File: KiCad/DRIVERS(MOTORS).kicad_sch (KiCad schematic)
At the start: 15 parts, among them M1 Motor_DC, M2 Motor_DC, M3 Motor_DC, U7 TB6612FNG, U8 TB6612FNG, U9 TB6612FNG

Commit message: Modificacio Labels
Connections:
- net +12V renamed VBAT
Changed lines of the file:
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@@
 		)
 	)
-	(global_label "+12V"
-		(shape bidirectional)
+	(global_label "VBAT"
+		(shape input)
 		(at 62.23 50.8 180)
 		(fields_autoplaced yes)
@@
 		)
 		(property "Intersheetrefs" "${INTERSHEET_REFS}"
-			(at 53.0535 50.8 0)
+			(at 55.4842 50.8 0)
 			(effects
 				(font
@@
 		)
 	)
-	(global_label "+12V"
-		(shape bidirectional)
+	(global_label "VBAT"
+		(shape input)
 		(at 55.88 60.96 180)
 		(fields_autoplaced yes)
@@
 		)
 		(property "Intersheetrefs" "${INTERSHEET_REFS}"
-			(at 46.7035 60.96 0)
+			(at 49.1342 60.96 0)
 			(effects
 				(font
@@
 		)
 	)
-	(global_label "+12V"
-		(shape bidirectional)
+	(global_label "VBAT"
+		(shape input)
 		(at 54.61 151.13 180)
 		(fields_autoplaced yes)
@@
 		)
 		(property "Intersheetrefs" "${INTERSHEET_REFS}"
-			(at 45.4335 151.13 0)
+			(at 47.8642 151.13 0)
 			(effects
 				(font
@@
 		)
 	)
-	(global_label "+12V"
-		(shape bidirectional)
+	(global_label "VBAT"
+		(shape input)
 		(at 180.34 87.63 180)
 		(fields_autoplaced yes)
@@
 		)
 		(property "Intersheetrefs" "${INTERSHEET_REFS}"
-			(at 171.1635 87.63 0)
-			(effects
-				(font
-					(size 1.27 1.27)
-				)
-				(justify right)
-				(hide yes)
-			)
-		)
-	)
-	(global_label "+12V"
-		(shape bidirectional)
+			(at 173.5942 87.63 0)
+			(effects
+				(font
+					(size 1.27 1.27)
+				)
+				(justify right)
+				(hide yes)
+			)
+		)
+	)
+	(global_label "VBAT"
+		(shape input)
 		(at 242.57 57.15 90)
 		(fields_autoplaced yes)
@@
 		)
 		(property "Intersheetrefs" "${INTERSHEET_REFS}"
-			(at 242.57 47.9735 90)
+			(at 242.57 50.4042 90)
 			(effects
 				(font
@@
 		)
 	)
-	(global_label "+12V"
-		(shape bidirectional)
+	(global_label "VBAT"
+		(shape input)
 		(at 60.96 140.97 180)
 		(fields_autoplaced yes)
@@
 		)
 		(property "Intersheetrefs" "${INTERSHEET_REFS}"
-			(at 51.7835 140.97 0)
-			(effects
-				(font
-					(size 1.27 1.27)
-				)
-				(justify right)
-				(hide yes)
-			)
-		)
-	)
-	(global_label "+12V"
-		(shape bidirectional)
+			(at 54.2142 140.97 0)
+			(effects
+				(font
+					(size 1.27 1.27)
+				)
+				(justify right)
+				(hide yes)
+			)
+		)
+	)
+	(global_label "VBAT"
+		(shape input)
 		(at 186.69 77.47 180)
 		(fields_autoplaced yes)
@@
 		)
 		(property "Intersheetrefs" "${INTERSHEET_REFS}"
-			(at 177.5135 77.47 0)
+			(at 179.9442 77.47 0)
 			(effects
 				(font
@@
 		)
 	)
-	(global_label "+12V"
-		(shape bidirectional)
+	(global_label "VBAT"
+		(shape input)
 		(at 123.19 114.3 90)
 		(fields_autoplaced yes)
@@
 		)
 		(property "Intersheetrefs" "${INTERSHEET_REFS}"
-			(at 123.19 105.1235 90)
-			(effects
-				(font
-					(size 1.27 1.27)
-				)
-				(justify left)
-				(hide yes)
-			)
-		)
-	)
-	(global_label "+12V"
-		(shape bidirectional)
+			(at 123.19 107.5542 90)
+			(effects
+				(font
+					(size 1.27 1.27)
+				)
+				(justify left)
+				(hide yes)
+			)
+		)
+	)
+	(global_label "VBAT"
+		(shape input)
 		(at 120.65 25.4 90)
 		(fields_autoplaced yes)
@@
 		)
 		(property "Intersheetrefs" "${INTERSHEET_REFS}"
-			(at 120.65 16.2235 90)
-			(effects
-				(font
+			(at 120.65 18.6542 90)
+			(effects
+				(font

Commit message: Modificacio
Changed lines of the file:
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@@
 	)
 	(global_label "GND"
-		(shape bidirectional)
+		(shape input)
 		(at 120.65 184.15 270)
 		(fields_autoplaced yes)
@@
 		)
 		(property "Intersheetrefs" "${INTERSHEET_REFS}"
-			(at 120.65 192.117 90)
+			(at 120.65 190.3515 90)
 			(effects
 				(font
@@
 	)
 	(global_label "GND"
-		(shape bidirectional)
+		(shape input)
 		(at 240.03 123.19 270)
 		(fields_autoplaced yes)
@@
 		)
 		(property "Intersheetrefs" "${INTERSHEET_REFS}"
-			(at 240.03 131.157 90)
+			(at 240.03 129.3915 90)
 			(effects
 				(font

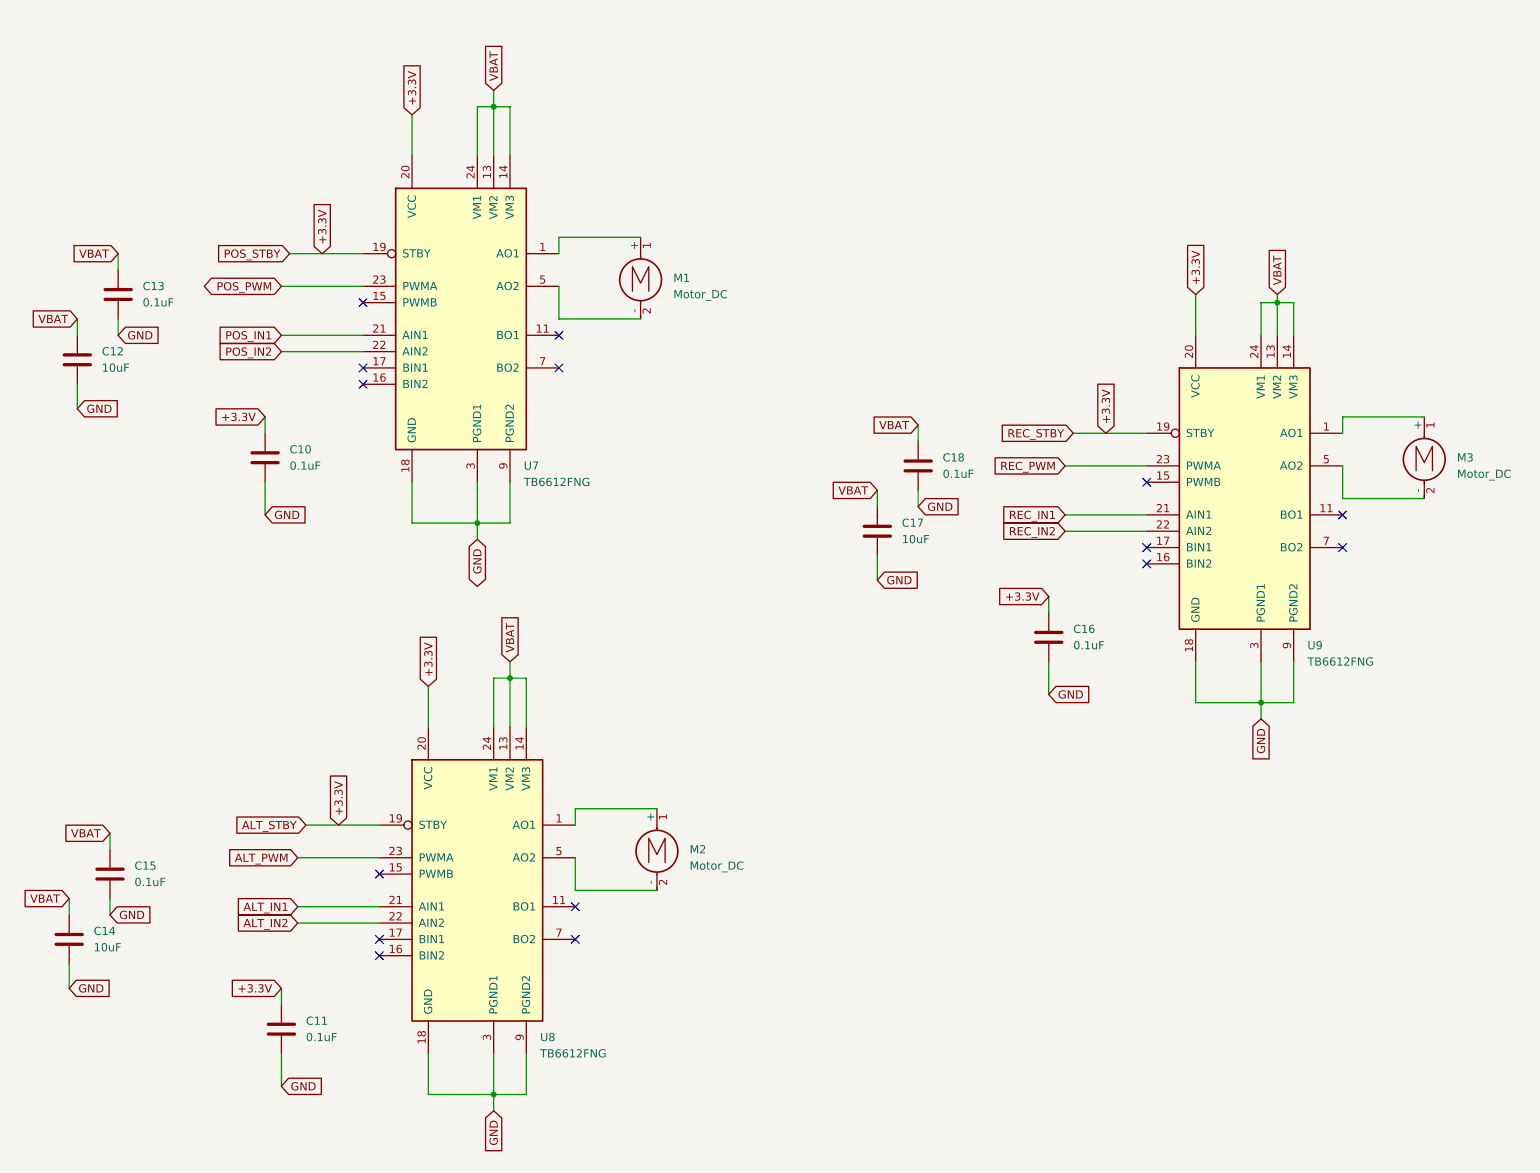
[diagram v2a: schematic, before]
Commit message: cambios mejora ERC
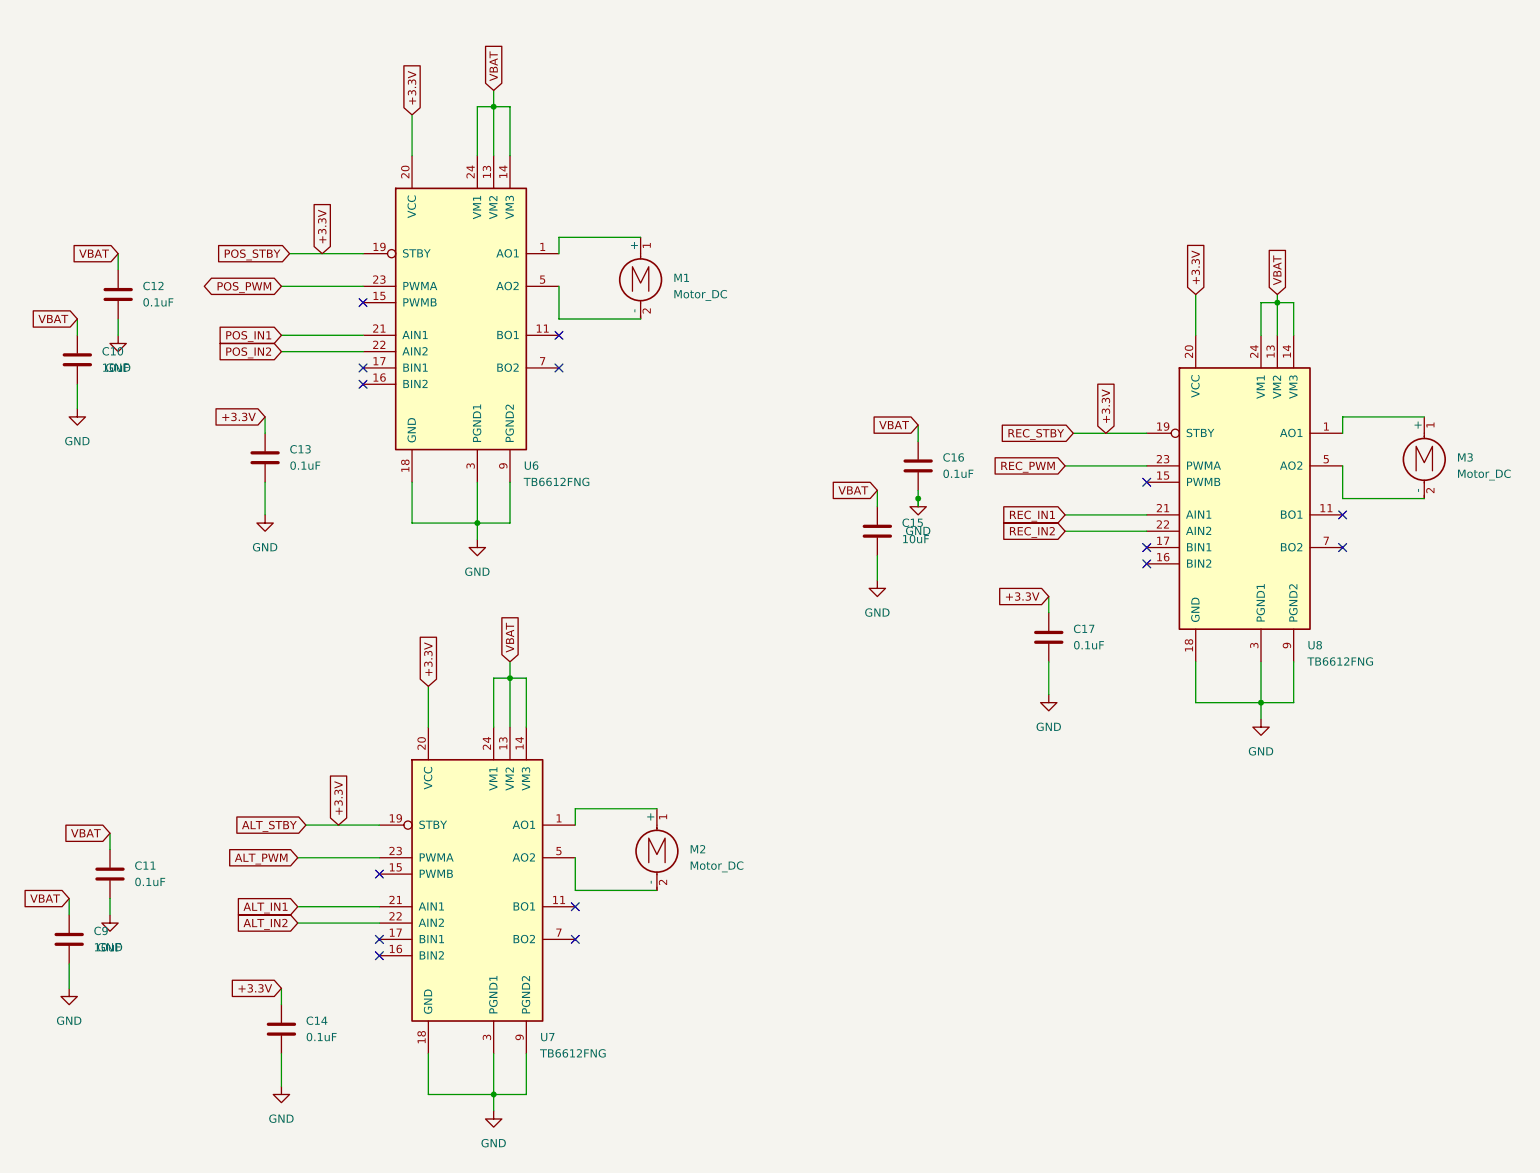
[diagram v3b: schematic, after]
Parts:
- renumbered C12 to C10, C15 to C11, C13 to C12, C10 to C13, C11 to C14, C17 to C15, C18 to C16, C16 to C17, C14 to C9, U7 to U6, U8 to U7, U9 to U8

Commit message: Cambio en la parte de motores y drivers
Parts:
- removed C11, C14, C16, C17: 0.1uF, symbol Device:C
- removed C15, C9: 10uF, symbol Device:C
- removed M3: Motor_DC, symbol Motor:Motor_DC
- removed U7, U8: TB6612FNG, Package_SO:SSOP-24_5.3x8.2mm_P0.65mm, symbol Driver_Motor:TB6612FNG
- added C4: 100nF, symbol Device:C
- added C5: 10uF, symbol Device:C
- added C6: 0.1uF, symbol Device:C
- added M4: Motor_DC, symbol Motor:Motor_DC
- added R1: 10k, symbol Device:R
- added R2, R3: 4.7k, symbol Device:R_US
- added R4, R5: 10k, symbol Device:R_US
- added U2: DRV8871DDA, Package_SO:SSOP-24_5.3x8.2mm_P0.65mm, symbol Driver_Motor:DRV8871DDA
- added U3: ATtiny1616-M, Package_DFN_QFN:VQFN-20-1EP_3x3mm_P0.4mm_EP1.7x1.7mm, symbol MCU_Microchip_ATtiny:ATtiny1616-M
- renumbered C13 to C1, C12 to C2, C10 to C3, U6 to U1
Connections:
- net +3.3V: now also C4.1, R2.1, R3.2, R4.1, R5.1, U3.2 (PA3), U3.4 (VCC)
- net ALT_IN1: now also U2.3 (IN1), U3.12 (PB2)
- net ALT_IN2: now also U2.2 (IN2), U3.11 (PB3)
- net GND: now also C4.2, C5.2, C6.2, R1.2, R4.2, U2.1 (GND), U2.7 (GND), U2.9 (GND), U3.21 (GND), U3.3 (GND)
- net POS_IN1: now also U3.6 (PA5)
- net POS_IN2: now also U3.7 (PA6)
- net POS_PWM: now also U3.5 (PA4)
- net REC_IN1: now also U1.17 (BIN1), U3.14 (PB0)
- net REC_IN2: now also U1.16 (BIN2), U3.13 (PB1)
- net REC_PWM: now also U1.15 (PWMB), U3.8 (PA7)
- net VBAT: now also C5.1, C6.1, U2.5 (VM)
- net at M2.1 (+): now also U1.11 (BO1), U1.12 (BO1)
- net at M2.2 (-): now also U1.7 (BO2), U1.8 (BO2)
- new net: R1.1, U2.4 (ILIM)
- new net: M4.1 (+), U2.6 (OUT1)
- new net: M4.2 (-), U2.8 (OUT2)
- new net MCU_SCL: R3.1, U3.1 (PA2)
- new net MCU_SDA: R2.2, U3.20 (PA1)
- new net UPDI / RESET: R5.2, U3.19 (~{RESET}/PA0)
- no-connect marks 15 -> 6
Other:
- moved on the sheet: C1, C2, C3

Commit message: Modificacions Micro
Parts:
- renumbered C3 to C10, C2 to C12, C1 to C13, C4 to C25, C5 to C26, C6 to C27, M4 to M3, R5 to R16, R3 to R17, R1 to R18, R4 to R19, R2 to R20, U3 to U11, U2 to U12, U1 to U6

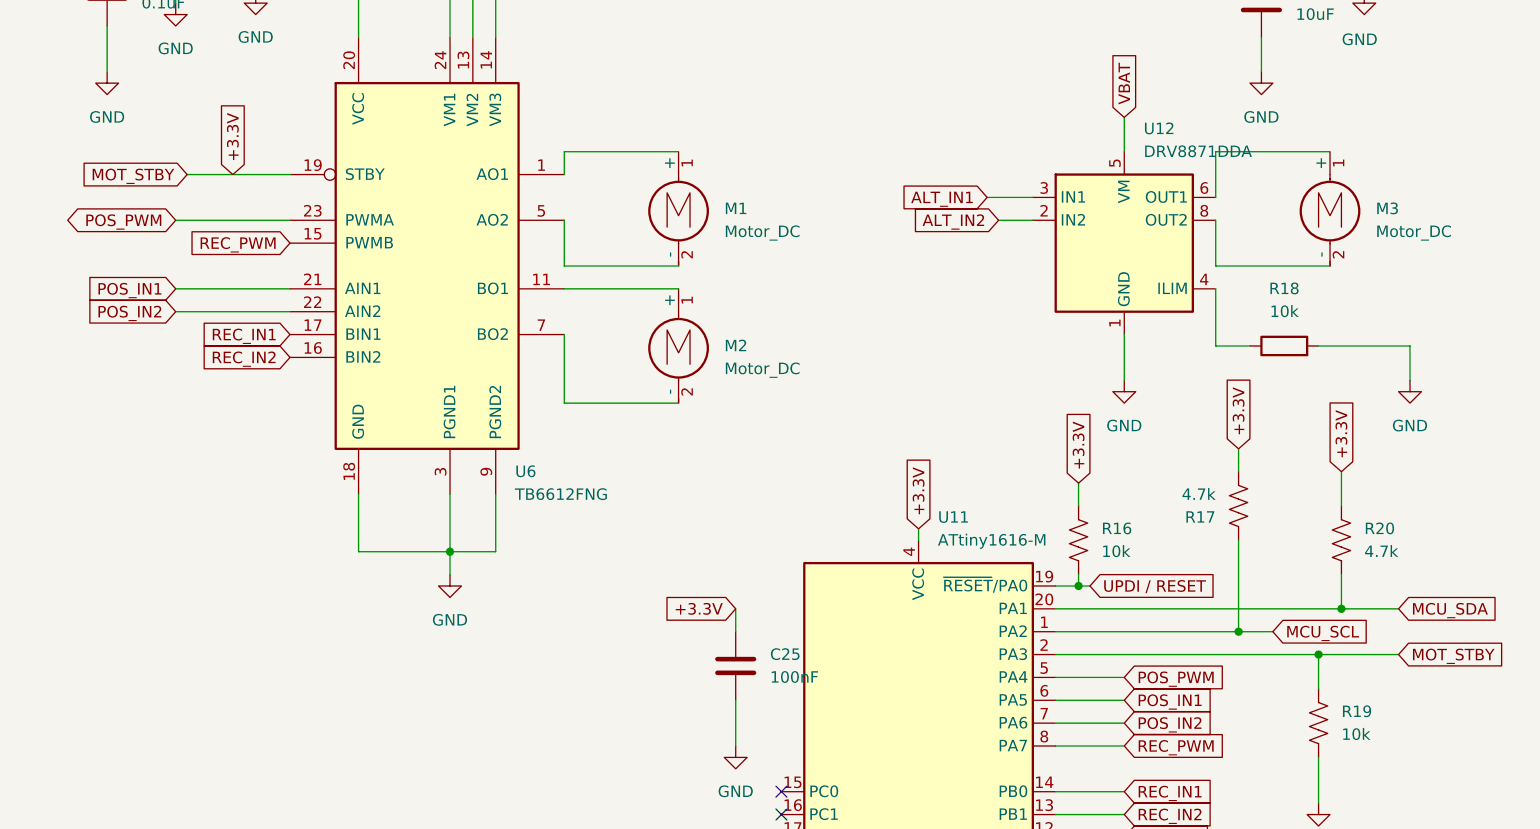
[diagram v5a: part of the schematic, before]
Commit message: Començat el LAYOUT
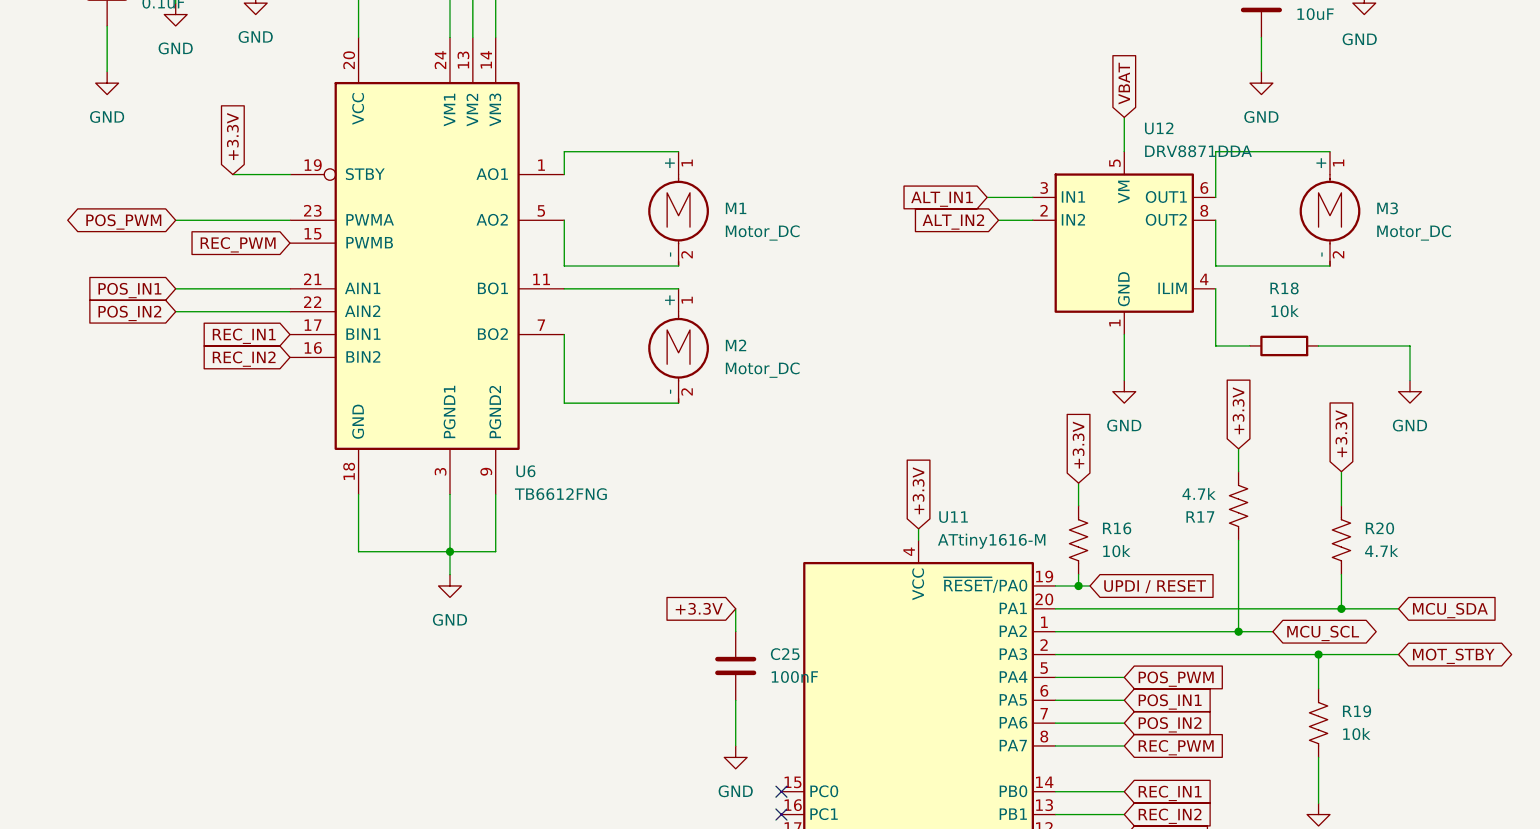
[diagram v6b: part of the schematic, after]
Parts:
- R16, R17, R18, R19, R20: footprint (none) -> Resistor_SMD:R_0805_2012Metric
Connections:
- net +3.3V: no longer R19.1, U11.2 (PA3)
- new net MOT_STBY: R19.1, U11.2 (PA3)
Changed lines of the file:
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@@
 	(wire
 		(pts
+			(xy 93.98 50.8) (xy 100.33 50.8)
+		)
+		(stroke
+			(width 0)
+			(type default)
+		)
+	)
+	(wire
+		(pts
 			(xy 215.9 48.26) (xy 203.2 48.26)
 		)
@@
 	(wire
 		(pts
-			(xy 88.9 50.8) (xy 100.33 50.8)
-		)
-		(stroke
-			(width 0)
-			(type default)
-		)
-	)
-	(wire
-		(pts
 			(xy 205.74 83.82) (xy 205.74 81.28)
 		)
@@
 	)
 	(global_label "MCU_SCL"
-		(shape input)
+		(shape bidirectional)
 		(at 209.55 101.6 0)
 		(fields_autoplaced yes)
@@
 		)
 		(property "Intersheetrefs" "${INTERSHEET_REFS}"
-			(at 221.0623 101.6 0)
+			(at 221.3606 101.6 0)
 			(effects
 				(font
@@
 	)
 	(global_label "MOT_STBY"
-		(shape input)
-		(at 88.9 50.8 180)
-		(fields_autoplaced yes)
-		(effects
-			(font
-				(size 1.27 1.27)
-			)
-			(justify right)
-		)
-		(property "Intersheetrefs" "${INTERSHEET_REFS}"
-			(at 76.662 50.8 0)
-			(effects
-				(font
-					(size 1.27 1.27)
-				)
-				(justify right)
-				(hide yes)
-			)
-		)
-	)
-	(global_label "MOT_STBY"
-		(shape input)
+		(shape bidirectional)
 		(at 223.52 104.14 0)
 		(fields_autoplaced yes)
@@
 		)
 		(property "Intersheetrefs" "${INTERSHEET_REFS}"
-			(at 235.758 104.14 0)
+			(at 236.0563 104.14 0)
 			(effects
 				(font
@@
 			)
 		)
-		(property "Footprint" ""
+		(property "Footprint" "Resistor_SMD:R_0805_2012Metric"
 			(at 210.82 71.628 90)
 			(effects
@@
 			)
 		)
-		(property "Footprint" ""
+		(property "Footprint" "Resistor_SMD:R_0805_2012Metric"
 			(at 204.724 87.376 90)
 			(effects
@@
 			)
 		)
-		(property "Footprint" ""
+		(property "Footprint" "Resistor_SMD:R_0805_2012Metric"
 			(at 218.186 91.694 90)
 			(effects
@@
 			)
 		)
-		(property "Footprint" ""
+		(property "Footprint" "Resistor_SMD:R_0805_2012Metric"
 			(at 188.976 91.694 90)
 			(effects
@@
 			)
 		)
-		(property "Footprint" ""
+		(property "Footprint" "Resistor_SMD:R_0805_2012Metric"
 			(at 215.646 112.014 90)
 			(effects
